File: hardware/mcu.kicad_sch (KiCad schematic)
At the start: 55 parts, among them J10 PRPC004SAAN-RC, J6 SBH11-NBPC-D05-SM-BK, J7 PRPC006SAAN-RC, J8 PRPC001DAAN-RC, J9 PRPC006SAAN-RC, U4 AT25SF081B-SSHD-B, U5 MCP9808, U6 STM32L552CETx, Y1 ECS-160-9-37-CKM-TR3, Y2 ABS05-32.768KHZ-9-T

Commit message: HW: Update components to be hand solderable
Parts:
- C10, C15, C19, C9: footprint Capacitor_SMD:C_0603_1608Metric -> Capacitor_SMD:C_0603_1608Metric_Pad1.08x0.95mm_HandSolder
- C11, C12, C13, C14, C16, C17, C18, C20, C21, C22: footprint perfect_footprints:0402_1005_perfect -> Capacitor_SMD:C_0402_1005Metric_Pad0.74x0.62mm_HandSolder
- FB2: footprint Resistor_SMD:R_0603_1608Metric -> Resistor_SMD:R_0603_1608Metric_Pad0.98x0.95mm_HandSolder
- LED4, LED5, LED6: footprint LED_SMD:LED_PLCC_2835 -> LED_SMD:LED_PLCC_2835_Handsoldering
- R14, R15, R16, R17, R18, R19, R20, R21, R22, R23, R24, R25, R26, R27, R28, R29: footprint perfect_footprints:0402_1005_perfect -> Resistor_SMD:R_0402_1005Metric_Pad0.72x0.64mm_HandSolder
- TVS10, TVS11, TVS2, TVS3, TVS4, TVS5, TVS6, TVS7, TVS8, TVS9: footprint perfect_footprints:0402_1005_perfect -> Diode_SMD:D_0402_1005Metric_Pad0.77x0.64mm_HandSolder
- U6: footprint Package_DFN_QFN:QFN-48-1EP_7x7mm_P0.5mm_EP3.5x3.5mm -> Package_QFP:LQFP-48_7x7mm_P0.5mm
- Y1: footprint Crystal:Crystal_SMD_2016-4Pin_2.0x1.6mm -> Crystal:Crystal_SMD_3225-4Pin_3.2x2.5mm_HandSoldering; Digi-Key Part Number 50-ECS-160-9-37-CKM-TR3CT-ND -> 50-ECS-160-9-33B-CKM-TR3CT-ND; Manufacturer Part Number ECS-160-9-37-CKM-TR3 -> ECS-160-9-33B-CKM-TR3
- Y2: footprint Crystal:Crystal_SMD_MicroCrystal_CM9V-T1A-2Pin_1.6x1.0mm -> Crystal:Crystal_SMD_MicroCrystal_CM9V-T1A-2Pin_1.6x1.0mm_HandSoldering
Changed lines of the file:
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@@
 			)
 		)
-		(property "Footprint" "perfect_footprints:0402_1005_perfect"
+		(property "Footprint" "Resistor_SMD:R_0402_1005Metric_Pad0.72x0.64mm_HandSolder"
 			(at 203.962 146.05 90)
 			(effects
@@
 			)
 		)
-		(property "Footprint" "perfect_footprints:0402_1005_perfect"
+		(property "Footprint" "Capacitor_SMD:C_0402_1005Metric_Pad0.74x0.62mm_HandSolder"
 			(at 174.2948 36.83 0)
 			(effects
@@
 			)
 		)
-		(property "Footprint" "Capacitor_SMD:C_0603_1608Metric"
+		(property "Footprint" "Capacitor_SMD:C_0603_1608Metric_Pad1.08x0.95mm_HandSolder"
 			(at 161.5948 36.83 0)
 			(effects
@@
 			)
 		)
-		(property "Footprint" "perfect_footprints:0402_1005_perfect"
+		(property "Footprint" "Diode_SMD:D_0402_1005Metric_Pad0.77x0.64mm_HandSolder"
 			(at 273.05 106.68 0)
 			(effects
@@
 			)
 		)
-		(property "Footprint" "perfect_footprints:0402_1005_perfect"
+		(property "Footprint" "Resistor_SMD:R_0402_1005Metric_Pad0.72x0.64mm_HandSolder"
 			(at 109.22 107.188 90)
 			(effects
@@
 			)
 		)
-		(property "Footprint" "perfect_footprints:0402_1005_perfect"
+		(property "Footprint" "Resistor_SMD:R_0402_1005Metric_Pad0.72x0.64mm_HandSolder"
 			(at 203.962 156.21 90)
 			(effects
@@
 			)
 		)
-		(property "Footprint" "Package_DFN_QFN:QFN-48-1EP_7x7mm_P0.5mm_EP3.5x3.5mm"
+		(property "Footprint" "Package_QFP:LQFP-48_7x7mm_P0.5mm"
 			(at 134.62 130.81 0)
 			(effects
@@
 			)
 		)
-		(property "Footprint" "perfect_footprints:0402_1005_perfect"
+		(property "Footprint" "Resistor_SMD:R_0402_1005Metric_Pad0.72x0.64mm_HandSolder"
 			(at 76.962 115.57 90)
 			(effects
@@
 			)
 		)
-		(property "Footprint" "Capacitor_SMD:C_0603_1608Metric"
+		(property "Footprint" "Capacitor_SMD:C_0603_1608Metric_Pad1.08x0.95mm_HandSolder"
 			(at 24.4348 129.54 0)
 			(effects
@@
 			)
 		)
-		(property "Footprint" "perfect_footprints:0402_1005_perfect"
+		(property "Footprint" "Resistor_SMD:R_0402_1005Metric_Pad0.72x0.64mm_HandSolder"
 			(at 180.34 69.088 90)
 			(effects
@@
 			)
 		)
-		(property "Footprint" "Capacitor_SMD:C_0603_1608Metric"
+		(property "Footprint" "Capacitor_SMD:C_0603_1608Metric_Pad1.08x0.95mm_HandSolder"
 			(at 98.0948 36.83 0)
 			(effects
@@
 			)
 		)
-		(property "Footprint" "perfect_footprints:0402_1005_perfect"
+		(property "Footprint" "Resistor_SMD:R_0402_1005Metric_Pad0.72x0.64mm_HandSolder"
 			(at 109.22 109.728 90)
 			(effects
@@
 			)
 		)
-		(property "Footprint" "perfect_footprints:0402_1005_perfect"
+		(property "Footprint" "Diode_SMD:D_0402_1005Metric_Pad0.77x0.64mm_HandSolder"
 			(at 255.27 106.68 0)
 			(effects
@@
 			)
 		)
-		(property "Footprint" "perfect_footprints:0402_1005_perfect"
+		(property "Footprint" "Diode_SMD:D_0402_1005Metric_Pad0.77x0.64mm_HandSolder"
 			(at 273.05 78.74 0)
 			(effects
@@
 			)
 		)
-		(property "Footprint" "perfect_footprints:0402_1005_perfect"
+		(property "Footprint" "Diode_SMD:D_0402_1005Metric_Pad0.77x0.64mm_HandSolder"
 			(at 264.16 106.68 0)
 			(effects
@@
 			)
 		)
-		(property "Footprint" "perfect_footprints:0402_1005_perfect"
+		(property "Footprint" "Capacitor_SMD:C_0402_1005Metric_Pad0.74x0.62mm_HandSolder"
 			(at 110.7948 36.83 0)
 			(effects
@@
 			)
 		)
-		(property "Footprint" "perfect_footprints:0402_1005_perfect"
+		(property "Footprint" "Diode_SMD:D_0402_1005Metric_Pad0.77x0.64mm_HandSolder"
 			(at 264.16 62.23 0)
 			(effects
@@
 			)
 		)
-		(property "Footprint" "Capacitor_SMD:C_0603_1608Metric"
+		(property "Footprint" "Capacitor_SMD:C_0603_1608Metric_Pad1.08x0.95mm_HandSolder"
 			(at 24.4348 171.45 0)
 			(effects
@@
 			)
 		)
-		(property "Footprint" "perfect_footprints:0402_1005_perfect"
+		(property "Footprint" "Resistor_SMD:R_0402_1005Metric_Pad0.72x0.64mm_HandSolder"
 			(at 257.81 159.258 90)
 			(effects
@@
 			)
 		)
-		(property "Footprint" "perfect_footprints:0402_1005_perfect"
+		(property "Footprint" "Resistor_SMD:R_0402_1005Metric_Pad0.72x0.64mm_HandSolder"
 			(at 109.22 104.648 90)
 			(effects
@@
 			)
 		)
-		(property "Footprint" "perfect_footprints:0402_1005_perfect"
+		(property "Footprint" "Resistor_SMD:R_0402_1005Metric_Pad0.72x0.64mm_HandSolder"
 			(at 109.22 112.268 90)
 			(effects
@@
 			)
 		)
-		(property "Footprint" "perfect_footprints:0402_1005_perfect"
+		(property "Footprint" "Capacitor_SMD:C_0402_1005Metric_Pad0.74x0.62mm_HandSolder"
 			(at 136.1948 36.83 0)
 			(effects
@@
 			)
 		)
-		(property "Footprint" "LED_SMD:LED_PLCC_2835"
+		(property "Footprint" "LED_SMD:LED_PLCC_2835_Handsoldering"
 			(at 270.51 157.48 0)
 			(effects
@@
 			)
 		)
-		(property "Footprint" "Crystal:Crystal_SMD_MicroCrystal_CM9V-T1A-2Pin_1.6x1.0mm"
+		(property "Footprint" "Crystal:Crystal_SMD_MicroCrystal_CM9V-T1A-2Pin_1.6x1.0mm_HandSoldering"
 			(at 71.12 73.66 0)
 			(effects
@@
 			)
 		)
-		(property "Footprint" "perfect_footprints:0402_1005_perfect"
+		(property "Footprint" "Capacitor_SMD:C_0402_1005Metric_Pad0.74x0.62mm_HandSolder"
 			(at 266.3952 30.48 0)
 			(effects
@@
 			)
 		)
-		(property "Footprint" "LED_SMD:LED_PLCC_2835"
+		(property "Footprint" "LED_SMD:LED_PLCC_2835_Handsoldering"
 			(at 270.51 153.67 0)
 			(effects
@@
 			)
 		)
-		(property "Footprint" "perfect_footprints:0402_1005_perfect"
+		(property "Footprint" "Capacitor_SMD:C_0402_1005Metric_Pad0.74x0.62mm_HandSolder"
 			(at 201.6252 36.83 0)
 			(effects
@@
 			)
 		)
-		(property "Footprint" "perfect_footprints:0402_1005_perfect"
+		(property "Footprint" "Diode_SMD:D_0402_1005Metric_Pad0.77x0.64mm_HandSolder"
 			(at 273.05 62.23 0)
 			(effects
@@
 			)
 		)
-		(property "Footprint" "perfect_footprints:0402_1005_perfect"
+		(property "Footprint" "Resistor_SMD:R_0402_1005Metric_Pad0.72x0.64mm_HandSolder"
 			(at 257.81 155.448 90)
 			(effects
@@
 			)
 		)
-		(property "Footprint" "perfect_footprints:0402_1005_perfect"
+		(property "Footprint" "Resistor_SMD:R_0402_1005Metric_Pad0.72x0.64mm_HandSolder"
 			(at 83.058 115.57 90)
 			(effects
@@
 			)
 		)
-		(property "Footprint" "perfect_footprints:0402_1005_perfect"
+		(property "Footprint" "Diode_SMD:D_0402_1005Metric_Pad0.77x0.64mm_HandSolder"
 			(at 255.27 132.08 0)
 			(effects
@@
 			)
 		)
-		(property "Footprint" "perfect_footprints:0402_1005_perfect"
+		(property "Footprint" "Capacitor_SMD:C_0402_1005Metric_Pad0.74x0.62mm_HandSolder"
 			(at 123.4948 36.83 0)
 			(effects
@@
 			)
 		)
-		(property "Footprint" "perfect_footprints:0402_1005_perfect"
+		(property "Footprint" "Diode_SMD:D_0402_1005Metric_Pad0.77x0.64mm_HandSolder"
 			(at 255.27 62.23 0)
 			(effects
@@
 			)
 		)
-		(property "Footprint" "perfect_footprints:0402_1005_perfect"
+		(property "Footprint" "Resistor_SMD:R_0402_1005Metric_Pad0.72x0.64mm_HandSolder"
 			(at 211.582 146.05 90)
 			(effects
@@
 			)
 		)
-		(property "Footprint" "perfect_footprints:0402_1005_perfect"
+		(property "Footprint" "Capacitor_SMD:C_0402_1005Metric_Pad0.74x0.62mm_HandSolder"
 			(at 77.7748 81.28 0)
 			(effects
@@
 			)
 		)
-		(property "Footprint" "perfect_footprints:0402_1005_perfect"
+		(property "Footprint" "Capacitor_SMD:C_0402_1005Metric_Pad0.74x0.62mm_HandSolder"
 			(at 30.1752 81.28 0)
 			(effects
@@
 			)
 		)
-		(property "Footprint" "perfect_footprints:0402_1005_perfect"
+		(property "Footprint" "Diode_SMD:D_0402_1005Metric_Pad0.77x0.64mm_HandSolder"
 			(at 264.16 132.08 0)
 			(effects
@@
 			)
 		)
-		(property "Footprint" "perfect_footprints:0402_1005_perfect"
+		(property "Footprint" "Resistor_SMD:R_0402_1005Metric_Pad0.72x0.64mm_HandSolder"
 			(at 270.002 25.4 90)
 			(effects
@@
 			)
 		)
-		(property "Footprint" "perfect_footprints:0402_1005_perfect"
+		(property "Footprint" "Resistor_SMD:R_0402_1005Metric_Pad0.72x0.64mm_HandSolder"
 			(at 257.81 163.068 90)
 			(effects
@@
 			)
 		)
-		(property "Footprint" "perfect_footprints:0402_1005_perfect"
+		(property "Footprint" "Capacitor_SMD:C_0402_1005Metric_Pad0.74x0.62mm_HandSolder"
 			(at 64.4652 81.28 0)
 			(effects
@@
 			)
 		)
-		(property "Footprint" "Resistor_SMD:R_0603_1608Metric"
+		(property "Footprint" "Resistor_SMD:R_0603_1608Metric_Pad0.98x0.95mm_HandSolder"
 			(at 187.96 30.988 90)
 			(effects
@@
 			)
 		)
-		(property "Footprint" "perfect_footprints:0402_1005_perfect"
+		(property "Footprint" "Diode_SMD:D_0402_1005Metric_Pad0.77x0.64mm_HandSolder"
 			(at 273.05 132.08 0)
 			(effects
@@
 			)
 		)
-		(property "Footprint" "LED_SMD:LED_PLCC_2835"
+		(property "Footprint" "LED_SMD:LED_PLCC_2835_Handsoldering"
 			(at 270.51 161.29 0)
 			(effects
@@
 			)
 		)
-		(property "Footprint" "Crystal:Crystal_SMD_2016-4Pin_2.0x1.6mm"
+		(property "Footprint" "Crystal:Crystal_SMD_3225-4Pin_3.2x2.5mm_HandSoldering"
 			(at 39.37 73.66 0)
 			(effects
@@
 			)
 		)
-		(property "Digi-Key Part Number" "50-ECS-160-9-37-CKM-TR3CT-ND"
+		(property "Digi-Key Part Number" "50-ECS-160-9-33B-CKM-TR3CT-ND"
 			(at 39.37 73.66 0)
 			(effects
@@
 			)
 		)
-		(property "Manufacturer Part Number" "ECS-160-9-37-CKM-TR3"
+		(property "Manufacturer Part Number" "ECS-160-9-33B-CKM-TR3"
 			(at 39.37 73.66 0)
 			(effects
@@
 			)
 		)
-		(property "Footprint" "perfect_footprints:0402_1005_perfect"
+		(property "Footprint" "Resistor_SMD:R_0402_1005Metric_Pad0.72x0.64mm_HandSolder"
 			(at 211.582 156.21 90)
 			(effects
@@
 			)
 		)
-		(property "Footprint" "perfect_footprints:0402_1005_perfect"
+		(property "Footprint" "Capacitor_SMD:C_0402_1005Metric_Pad0.74x0.62mm_HandSolder"
 			(at 53.0352 81.28 0)
 			(effects
@@
 			)
 		)
-		(property "Footprint" "perfect_footprints:0402_1005_perfect"
+		(property "Footprint" "Resistor_SMD:R_0402_1005Metric_Pad0.72x0.64mm_HandSolder"
 			(at 180.34 71.628 90)
 			(effects

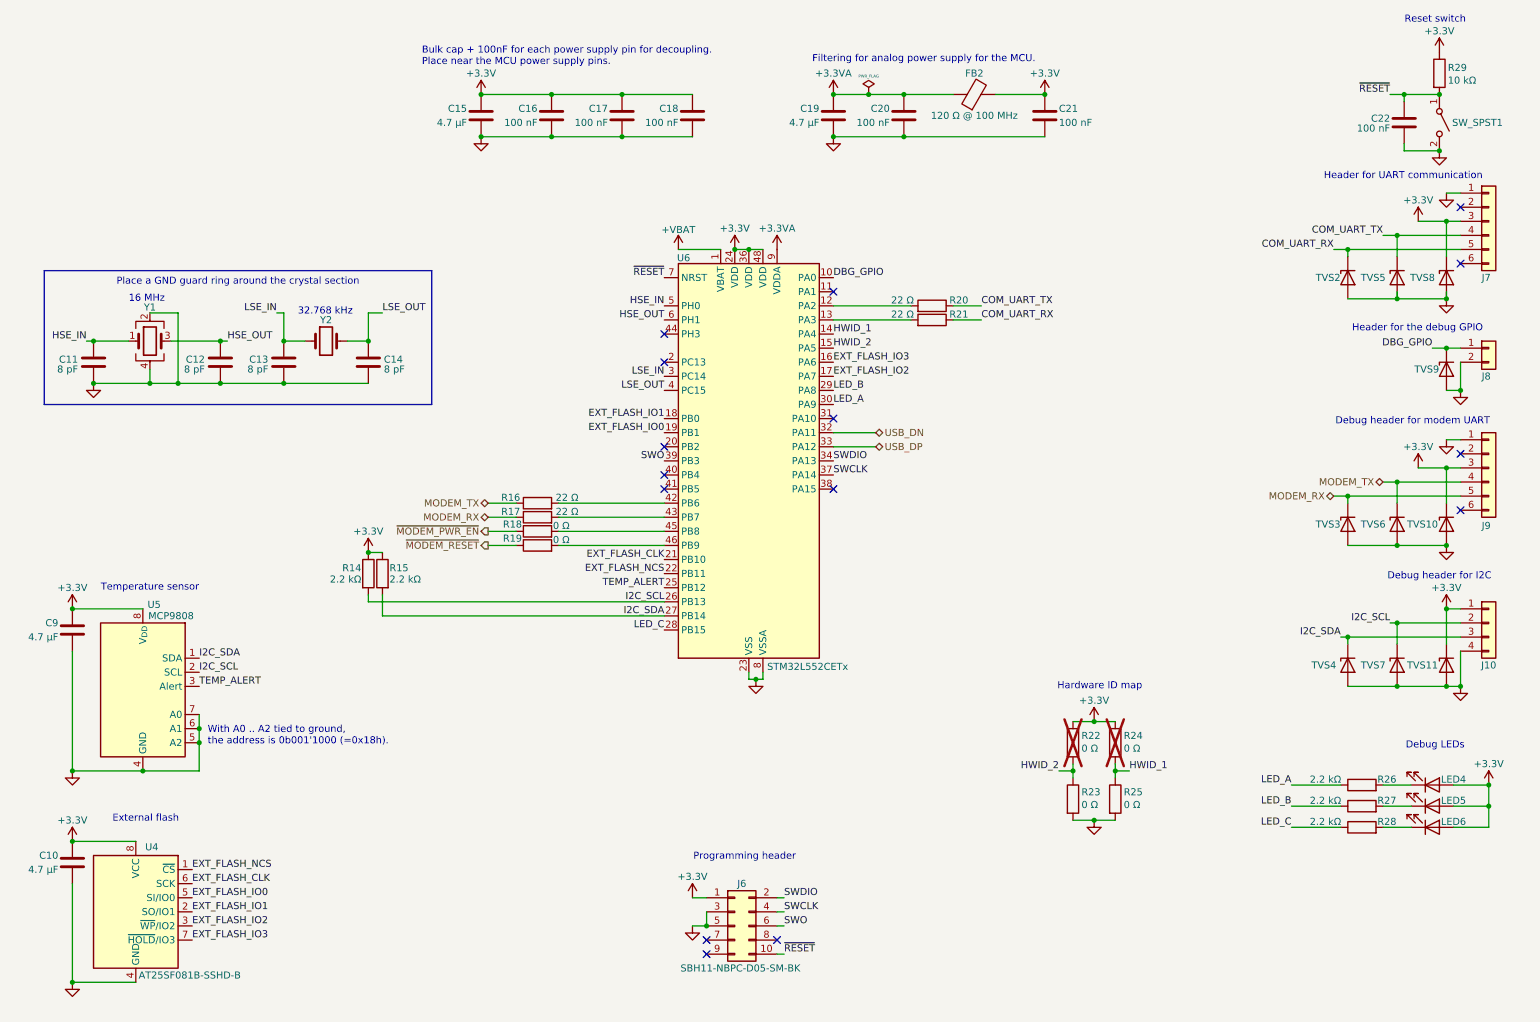
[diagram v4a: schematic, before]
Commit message: HW: Update components, change footprints to handsolder versions, finish power
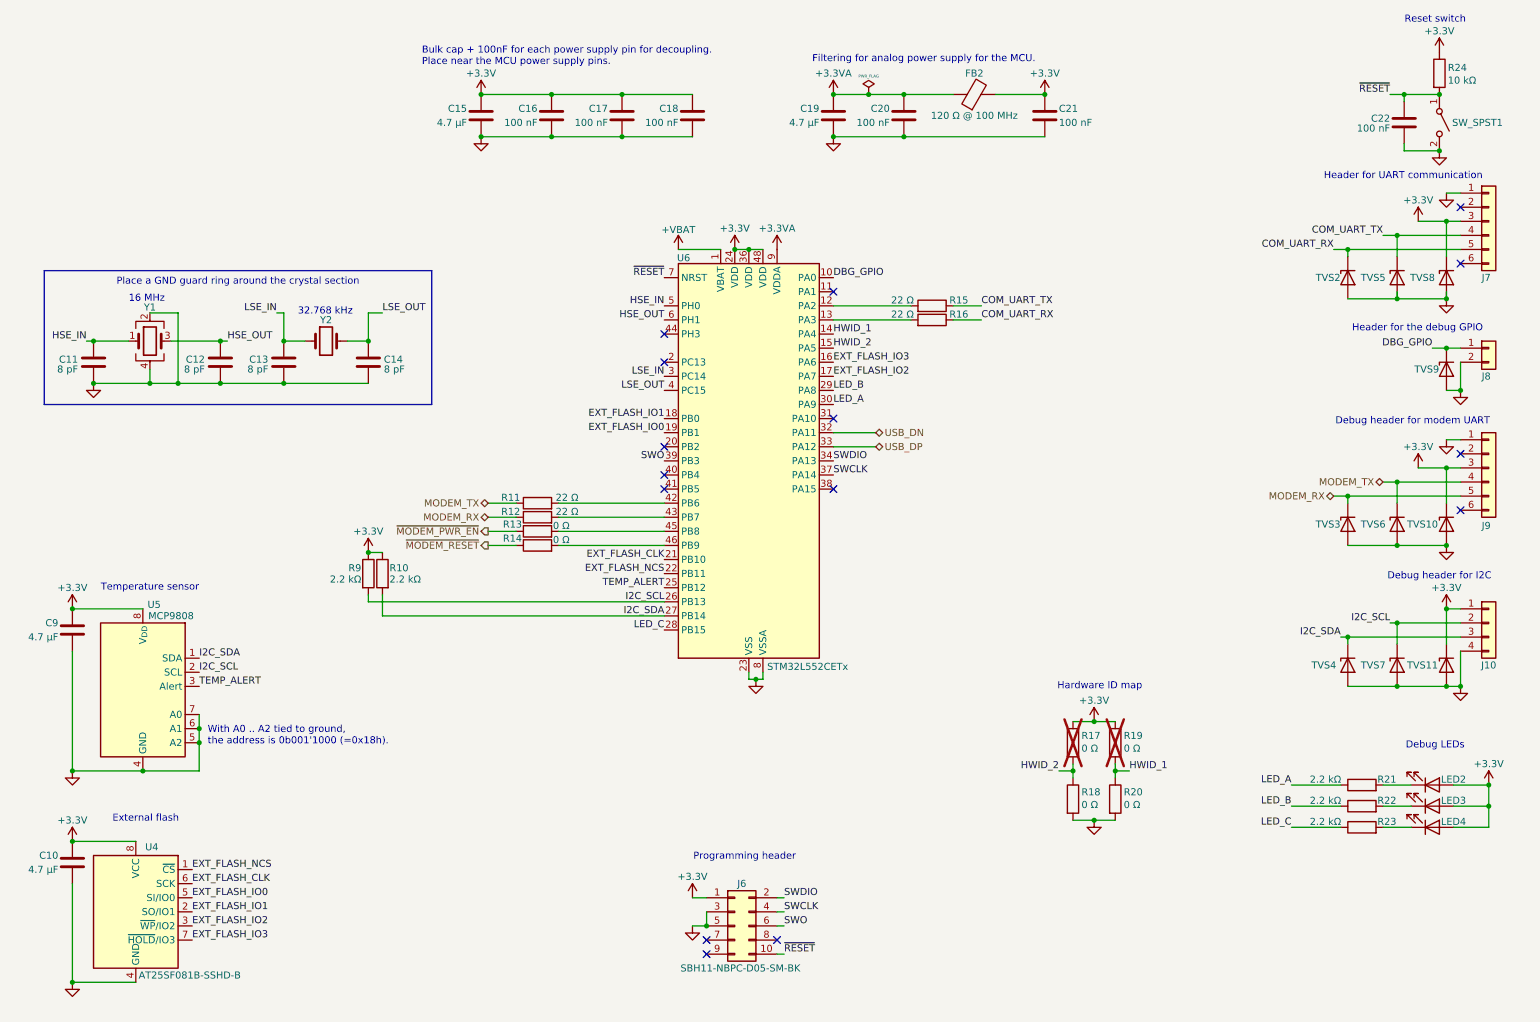
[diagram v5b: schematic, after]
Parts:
- R10: renamed from R15; Digi-Key Part Number 311-2.20KLRCT-ND -> 732-560112110087CT-ND; Manufacturer YAGEO -> Würth Elektronik; Manufacturer Part Number RC0402FR-072K2L -> 560112110087
- R11: renamed from R16; Digi-Key Part Number 311-22.0LRCT-ND -> 732-560112110046CT-ND; Manufacturer YAGEO -> Würth Elektronik; Manufacturer Part Number RC0402FR-0722RL -> 560112110046
- R12: renamed from R17; Digi-Key Part Number 311-22.0LRCT-ND -> 732-560112110046CT-ND; Manufacturer YAGEO -> Würth Elektronik; Manufacturer Part Number RC0402FR-0722RL -> 560112110046
- R13: renamed from R18; Digi-Key Part Number 311-0.0JRCT-ND -> 732-560112110001CT-ND; Manufacturer YAGEO -> Würth Elektronik; Manufacturer Part Number RC0402JR-070RL -> 560112110001
- R14: renamed from R19; Digi-Key Part Number 311-0.0JRCT-ND -> 732-560112110001CT-ND; Manufacturer YAGEO -> Würth Elektronik; Manufacturer Part Number RC0402JR-070RL -> 560112110001
- R15: renamed from R20; Digi-Key Part Number 311-22.0LRCT-ND -> 732-560112110046CT-ND; Manufacturer YAGEO -> Würth Elektronik; Manufacturer Part Number RC0402FR-0722RL -> 560112110046
- R16: renamed from R21; Digi-Key Part Number 311-22.0LRCT-ND -> 732-560112110046CT-ND; Manufacturer YAGEO -> Würth Elektronik; Manufacturer Part Number RC0402FR-0722RL -> 560112110046
- R17: renamed from R22; Digi-Key Part Number 311-0.0JRCT-ND -> 732-560112110001CT-ND; Manufacturer YAGEO -> Würth Elektronik; Manufacturer Part Number RC0402JR-070RL -> 560112110001
- R18: renamed from R23; Digi-Key Part Number 311-0.0JRCT-ND -> 732-560112110001CT-ND; Manufacturer YAGEO -> Würth Elektronik; Manufacturer Part Number RC0402JR-070RL -> 560112110001
- R19: renamed from R24; Digi-Key Part Number 311-0.0JRCT-ND -> 732-560112110001CT-ND; Manufacturer YAGEO -> Würth Elektronik; Manufacturer Part Number RC0402JR-070RL -> 560112110001
- R20: renamed from R25; Digi-Key Part Number 311-0.0JRCT-ND -> 732-560112110001CT-ND; Manufacturer YAGEO -> Würth Elektronik; Manufacturer Part Number RC0402JR-070RL -> 560112110001
- R21: renamed from R26; Digi-Key Part Number 311-2.20KLRCT-ND -> 732-560112110087CT-ND; Manufacturer YAGEO -> Würth Elektronik; Manufacturer Part Number RC0402FR-072K2L -> 560112110087
- R22: renamed from R27; Digi-Key Part Number 311-2.20KLRCT-ND -> 732-560112110087CT-ND; Manufacturer YAGEO -> Würth Elektronik; Manufacturer Part Number RC0402FR-072K2L -> 560112110087
- R23: renamed from R28; Digi-Key Part Number 311-2.20KLRCT-ND -> 732-560112110087CT-ND; Manufacturer YAGEO -> Würth Elektronik; Manufacturer Part Number RC0402FR-072K2L -> 560112110087
- R24: renamed from R29; Digi-Key Part Number 311-10.0KLRCT-ND -> 732-560112110020CT-ND; Manufacturer YAGEO -> Würth Elektronik; Manufacturer Part Number RC0402FR-0710KL -> 560112110020
- R9: renamed from R14; Digi-Key Part Number 311-2.20KLRCT-ND -> 732-560112110087CT-ND; Manufacturer YAGEO -> Würth Elektronik; Manufacturer Part Number RC0402FR-072K2L -> 560112110087
- renumbered LED4 to LED2, LED5 to LED3, LED6 to LED4
